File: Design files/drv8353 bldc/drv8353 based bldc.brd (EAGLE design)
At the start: 127 x 127 mm, 117 parts, among them IC1 DRV8353RSRGZT, J3 2X6 FEMALE, J4 B06B-HCMKK

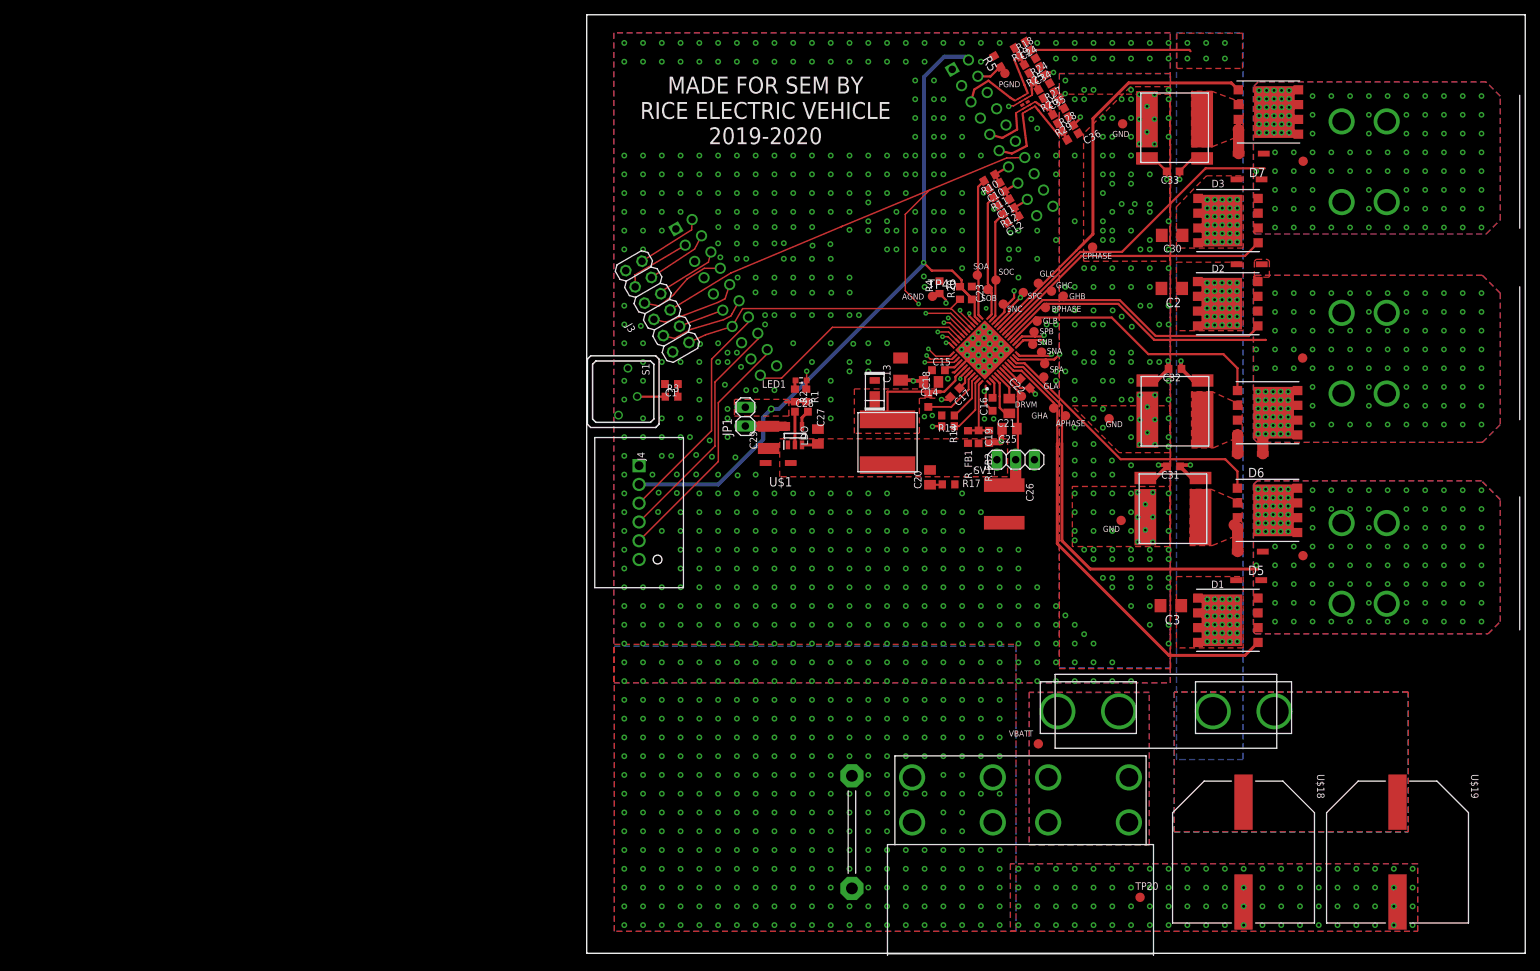
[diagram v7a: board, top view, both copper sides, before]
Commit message: replaces fets with ones we can actually get (are also 100v capable instead of 80)
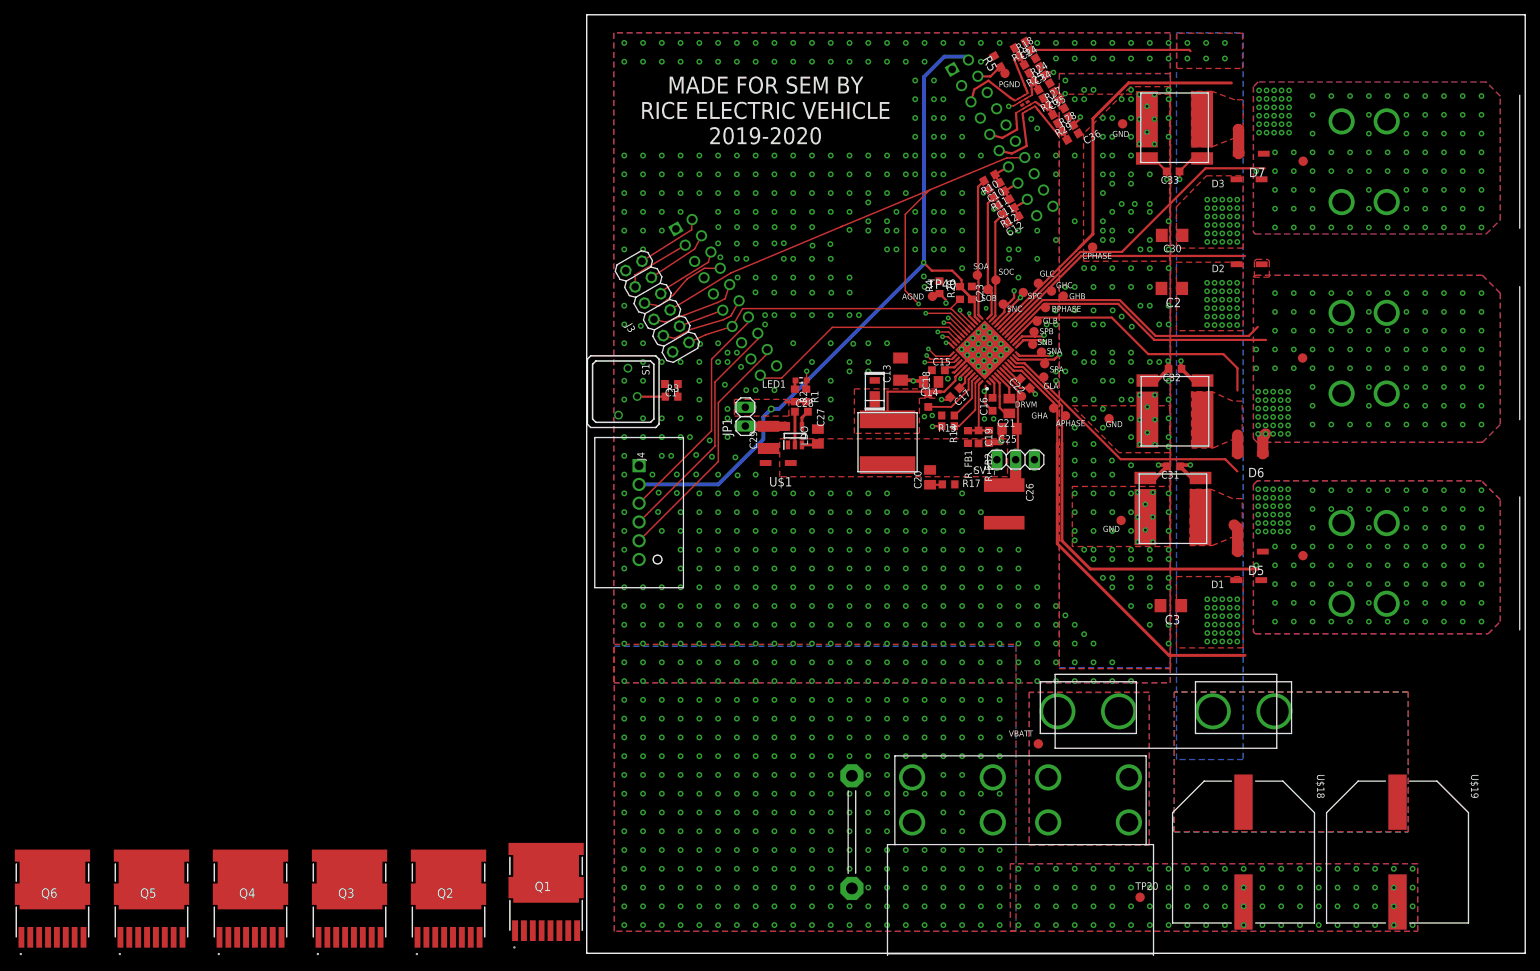
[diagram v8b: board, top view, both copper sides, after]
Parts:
- removed U$14, U$20, U$21, U$22, U$23, U$24: NVMTS1D2N08H, REV BLDC:PQFN88
- added Q1, Q2, Q3, Q4, Q5, Q6: FDBL86062-F085, SamacSys_Parts:H-PSOF8L-11.68X9.80_1
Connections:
- net APHASE: now also Q1.S2, Q1.S3, Q1.S4, Q1.S5, Q1.S6, Q1.S7, Q1.S8, Q2.D, Q2.D10, Q2.D11, Q2.D12, Q2.D13; no longer U$14.S1, U$14.S2, U$14.S3, U$20.D1, U$20.D2, U$20.D3, U$20.D4, U$20.DT
- net BPHASE: now also Q3.D, Q3.D10, Q3.D11, Q3.D12, Q3.D13, Q4.S2, Q4.S3, Q4.S4, Q4.S5, Q4.S6, Q4.S7, Q4.S8; no longer U$21.D1, U$21.D2, U$21.D3, U$21.D4, U$21.DT, U$22.S1, U$22.S2, U$22.S3
- net CPHASE: now also Q5.S2, Q5.S3, Q5.S4, Q5.S5, Q5.S6, Q5.S7, Q5.S8; no longer U$23.S1, U$23.S2, U$23.S3, U$24.D1, U$24.D2, U$24.D3, U$24.D4, U$24.DT
- net GHA: now also Q1.G; no longer U$14.G
- net GHB: now also Q4.G; no longer U$22.G
- net GHC: now also Q5.G; no longer U$23.G
- net GLA: now also Q2.G; no longer U$20.G
- net GLB: now also Q3.G; no longer U$21.G
- net GLC: now also Q6.G; no longer U$24.G
- net N$22: now also Q3.S2, Q3.S3, Q3.S4, Q3.S5, Q3.S6, Q3.S7, Q3.S8; no longer U$21.S1, U$21.S2, U$21.S3
- net N$24: now also Q2.S2, Q2.S3, Q2.S4, Q2.S5, Q2.S6, Q2.S7, Q2.S8; no longer U$20.S1, U$20.S2, U$20.S3
- net N$27: no longer U$24.S1, U$24.S2, U$24.S3
- net VDRAIN: now also Q1.D, Q1.D10, Q1.D11, Q1.D12, Q1.D13, Q4.D, Q4.D10, Q4.D11, Q4.D12, Q4.D13, Q5.D, Q5.D10, Q5.D11, Q5.D12, Q5.D13; no longer U$14.D1, U$14.D2, U$14.D3, U$14.D4, U$14.DT, U$22.D1, U$22.D2, U$22.D3, U$22.D4, U$22.DT, U$23.D1, U$23.D2, U$23.D3, U$23.D4, U$23.DT
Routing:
- net GHA: track 63.4 -> 60.3 mm
- net GLA: track 40.3 -> 37.8 mm
- net GHC: track 40.4 -> 37.9 mm
- net GLC: track 56.6 -> 54.8 mm
- net GLB: track 39.3 -> 38.8 mm
